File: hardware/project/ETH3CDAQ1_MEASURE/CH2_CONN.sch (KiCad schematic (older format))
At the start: 1 part, among them J1201 Conn_02x10_Odd_Even

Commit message: PCB layout
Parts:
- renumbered J1201 to J1101
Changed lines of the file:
@@
 AR Path="/5FC84995/5FE331B2" Ref="J?"  Part="1"
 AR Path="/5FDF6197/5FE331B2" Ref="J?"  Part="1"
-AR Path="/5FE2FF08/5FE331B2" Ref="J1201"  Part="1"
-F 0 "J1201" H 5400 3517 50  0000 C CNN
+AR Path="/5FE2FF08/5FE331B2" Ref="J1101"  Part="1"
+F 0 "J1101" H 5400 3517 50  0000 C CNN
 F 1 "Conn_02x10_Odd_Even" H 5400 3426 50  0000 C CNN
 F 2 "Connector_PinSocket_2.54mm:PinSocket_2x10_P2.54mm_Vertical" H 5350 2900 50  0001 C CNN
@@
 P 5150 2600
 AR Path="/5FDF6197/5FE331B8" Ref="#PWR?"  Part="1"
-AR Path="/5FE2FF08/5FE331B8" Ref="#PWR01202"  Part="1"
-F 0 "#PWR01202" H 5150 2350 50  0001 C CNN
+AR Path="/5FE2FF08/5FE331B8" Ref="#PWR01102"  Part="1"
+F 0 "#PWR01102" H 5150 2350 50  0001 C CNN
 F 1 "GND" V 5150 2450 50  0000 R CNN
 F 2 "" H 5150 2600 50  0001 C CNN
@@
 P 5150 2700
 AR Path="/5FDF6197/5FE331BE" Ref="#PWR?"  Part="1"
-AR Path="/5FE2FF08/5FE331BE" Ref="#PWR01203"  Part="1"
-F 0 "#PWR01203" H 5150 2450 50  0001 C CNN
+AR Path="/5FE2FF08/5FE331BE" Ref="#PWR01103"  Part="1"
+F 0 "#PWR01103" H 5150 2450 50  0001 C CNN
 F 1 "GND" V 5150 2550 50  0000 R CNN
 F 2 "" H 5150 2700 50  0001 C CNN
@@
 P 5650 2700
 AR Path="/5FDF6197/5FE331C4" Ref="#PWR?"  Part="1"
-AR Path="/5FE2FF08/5FE331C4" Ref="#PWR01208"  Part="1"
-F 0 "#PWR01208" H 5650 2450 50  0001 C CNN
+AR Path="/5FE2FF08/5FE331C4" Ref="#PWR01108"  Part="1"
+F 0 "#PWR01108" H 5650 2450 50  0001 C CNN
 F 1 "GND" V 5650 2550 50  0000 R CNN
 F 2 "" H 5650 2700 50  0001 C CNN
@@
 P 5150 2500
 AR Path="/5FDF6197/5FE331CA" Ref="#PWR?"  Part="1"
-AR Path="/5FE2FF08/5FE331CA" Ref="#PWR01201"  Part="1"
-F 0 "#PWR01201" H 5150 2250 50  0001 C CNN
+AR Path="/5FE2FF08/5FE331CA" Ref="#PWR01101"  Part="1"
+F 0 "#PWR01101" H 5150 2250 50  0001 C CNN
 F 1 "GND" V 5150 2350 50  0000 R CNN
 F 2 "" H 5150 2500 50  0001 C CNN
@@
 P 5150 3100
 AR Path="/5FDF6197/5FE331E4" Ref="#PWR?"  Part="1"
-AR Path="/5FE2FF08/5FE331E4" Ref="#PWR01204"  Part="1"
-F 0 "#PWR01204" H 5150 2850 50  0001 C CNN
+AR Path="/5FE2FF08/5FE331E4" Ref="#PWR01104"  Part="1"
+F 0 "#PWR01104" H 5150 2850 50  0001 C CNN
 F 1 "GND" V 5150 2950 50  0000 R CNN
 F 2 "" H 5150 3100 50  0001 C CNN
@@
 P 5650 3100
 AR Path="/5FDF6197/5FE331EA" Ref="#PWR?"  Part="1"
-AR Path="/5FE2FF08/5FE331EA" Ref="#PWR01209"  Part="1"
-F 0 "#PWR01209" H 5650 2850 50  0001 C CNN
+AR Path="/5FE2FF08/5FE331EA" Ref="#PWR01109"  Part="1"
+F 0 "#PWR01109" H 5650 2850 50  0001 C CNN
 F 1 "GND" V 5650 2950 50  0000 R CNN
 F 2 "" H 5650 3100 50  0001 C CNN
@@
 P 5150 3200
 AR Path="/5FDF6197/5FE331F0" Ref="#PWR?"  Part="1"
-AR Path="/5FE2FF08/5FE331F0" Ref="#PWR01205"  Part="1"
-F 0 "#PWR01205" H 5150 3050 50  0001 C CNN
+AR Path="/5FE2FF08/5FE331F0" Ref="#PWR01105"  Part="1"
+F 0 "#PWR01105" H 5150 3050 50  0001 C CNN
 F 1 "+3.3V" V 5150 3350 50  0000 L CNN
 F 2 "" H 5150 3200 50  0001 C CNN
@@
 P 5650 3200
 AR Path="/5FDF6197/5FE331F6" Ref="#PWR?"  Part="1"
-AR Path="/5FE2FF08/5FE331F6" Ref="#PWR01210"  Part="1"
-F 0 "#PWR01210" H 5650 3050 50  0001 C CNN
+AR Path="/5FE2FF08/5FE331F6" Ref="#PWR01110"  Part="1"
+F 0 "#PWR01110" H 5650 3050 50  0001 C CNN
 F 1 "+3.3V" V 5650 3350 50  0000 L CNN
 F 2 "" H 5650 3200 50  0001 C CNN
@@
 P 5150 3300
 AR Path="/5FDF6197/5FE331FC" Ref="#PWR?"  Part="1"
-AR Path="/5FE2FF08/5FE331FC" Ref="#PWR01206"  Part="1"
-F 0 "#PWR01206" H 5150 3150 50  0001 C CNN
+AR Path="/5FE2FF08/5FE331FC" Ref="#PWR01106"  Part="1"
+F 0 "#PWR01106" H 5150 3150 50  0001 C CNN
 F 1 "+9V" V 5150 3450 50  0000 L CNN
 F 2 "" H 5150 3300 50  0001 C CNN
@@
 P 5650 3300
 AR Path="/5FDF6197/5FE33202" Ref="#PWR?"  Part="1"
-AR Path="/5FE2FF08/5FE33202" Ref="#PWR01211"  Part="1"
-F 0 "#PWR01211" H 5650 3150 50  0001 C CNN
+AR Path="/5FE2FF08/5FE33202" Ref="#PWR01111"  Part="1"
+F 0 "#PWR01111" H 5650 3150 50  0001 C CNN
 F 1 "+5V" V 5650 3450 50  0000 L CNN
 F 2 "" H 5650 3300 50  0001 C CNN
@@
 P 5150 3400
 AR Path="/5FDF6197/5FE33208" Ref="#PWR?"  Part="1"
-AR Path="/5FE2FF08/5FE33208" Ref="#PWR01207"  Part="1"
-F 0 "#PWR01207" H 5150 3250 50  0001 C CNN
+AR Path="/5FE2FF08/5FE33208" Ref="#PWR01107"  Part="1"
+F 0 "#PWR01107" H 5150 3250 50  0001 C CNN
 F 1 "-18V" V 5150 3550 50  0000 L CNN
 F 2 "" H 5150 3400 50  0001 C CNN
@@
 P 5650 3400
 AR Path="/5FDF6197/5FE3320E" Ref="#PWR?"  Part="1"
-AR Path="/5FE2FF08/5FE3320E" Ref="#PWR01212"  Part="1"
-F 0 "#PWR01212" H 5650 3250 50  0001 C CNN
+AR Path="/5FE2FF08/5FE3320E" Ref="#PWR01112"  Part="1"
+F 0 "#PWR01112" H 5650 3250 50  0001 C CNN
 F 1 "+18V" V 5650 3550 50  0000 L CNN
 F 2 "" H 5650 3400 50  0001 C CNN

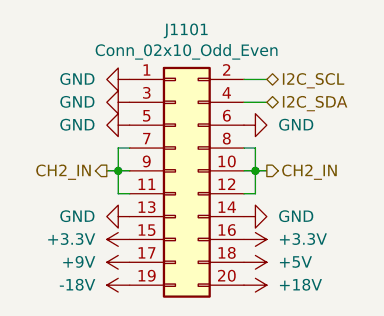
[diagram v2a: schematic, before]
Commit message: Started development of first current measurement module. Added CAN to the DAQ module.
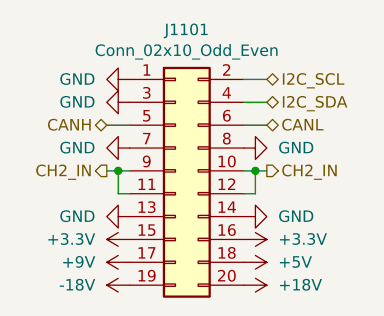
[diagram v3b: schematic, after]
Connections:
- net CH2_IN: no longer J1101.7 (Pin_7), J1101.8 (Pin_8)
- net GND: now also J1101.7 (Pin_7), J1101.8 (Pin_8); no longer J1101.5 (Pin_5), J1101.6 (Pin_6)
- new net CANH: J1101.5 (Pin_5)
- new net CANL: J1101.6 (Pin_6)
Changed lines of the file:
@@
 $Descr A4 11693 8268
 encoding utf-8
-Sheet 12 15
+Sheet 11 15
 Title ""
 Date ""
@@
 	0    1    1    0
 $EndComp
-$Comp
-L power:GND #PWR?
-U 1 1 5FE331BE
-P 5150 2700
-AR Path="/5FDF6197/5FE331BE" Ref="#PWR?"  Part="1"
-AR Path="/5FE2FF08/5FE331BE" Ref="#PWR01103"  Part="1"
-F 0 "#PWR01103" H 5150 2450 50  0001 C CNN
-F 1 "GND" V 5150 2550 50  0000 R CNN
-F 2 "" H 5150 2700 50  0001 C CNN
-F 3 "" H 5150 2700 50  0001 C CNN
-	1    5150 2700
-	0    1    1    0
-$EndComp
-$Comp
-L power:GND #PWR?
-U 1 1 5FE331C4
-P 5650 2700
-AR Path="/5FDF6197/5FE331C4" Ref="#PWR?"  Part="1"
-AR Path="/5FE2FF08/5FE331C4" Ref="#PWR01108"  Part="1"
-F 0 "#PWR01108" H 5650 2450 50  0001 C CNN
-F 1 "GND" V 5650 2550 50  0000 R CNN
-F 2 "" H 5650 2700 50  0001 C CNN
-F 3 "" H 5650 2700 50  0001 C CNN
-	1    5650 2700
-	0    -1   -1   0
-$EndComp
-$Comp
-L power:GND #PWR?
-U 1 1 5FE331CA
-P 5150 2500
-AR Path="/5FDF6197/5FE331CA" Ref="#PWR?"  Part="1"
-AR Path="/5FE2FF08/5FE331CA" Ref="#PWR01101"  Part="1"
-F 0 "#PWR01101" H 5150 2250 50  0001 C CNN
-F 1 "GND" V 5150 2350 50  0000 R CNN
-F 2 "" H 5150 2500 50  0001 C CNN
-F 3 "" H 5150 2500 50  0001 C CNN
-	1    5150 2500
-	0    1    1    0
-$EndComp
 Text HLabel 5750 2500 2    50   BiDi ~ 0
 I2C_SCL
@@
 	5650 2500 5750 2500
 Wire Wire Line
-	5650 2800 5700 2800
-Wire Wire Line
-	5700 2800 5700 2900
-Wire Wire Line
 	5700 3000 5650 3000
 Wire Wire Line
@@
 Wire Wire Line
 	5700 2900 5700 3000
-Wire Wire Line
-	5150 2800 5100 2800
-Wire Wire Line
-	5100 2800 5100 2900
 Wire Wire Line
 	5100 3000 5150 3000
@@
 	0    1    1    0
 $EndComp
+Wire Wire Line
+	5650 2700 5750 2700
+Wire Wire Line
+	5150 2700 5050 2700
+Text HLabel 5050 2700 0    50   BiDi ~ 0
+CANH
+Text HLabel 5750 2700 2    50   BiDi ~ 0
+CANL
+$Comp
+L power:GND #PWR?
+U 1 1 5FE5AC8A
+P 5150 2800
+AR Path="/5FDF6197/5FE5AC8A" Ref="#PWR?"  Part="1"
+AR Path="/5FE2FF08/5FE5AC8A" Ref="#PWR01103"  Part="1"
+F 0 "#PWR01103" H 5150 2550 50  0001 C CNN
+F 1 "GND" V 5150 2650 50  0000 R CNN
+F 2 "" H 5150 2800 50  0001 C CNN
+F 3 "" H 5150 2800 50  0001 C CNN
+	1    5150 2800
+	0    1    1    0
+$EndComp
+$Comp
+L power:GND #PWR?
+U 1 1 5FE5AE75
+P 5650 2800
+AR Path="/5FDF6197/5FE5AE75" Ref="#PWR?"  Part="1"
+AR Path="/5FE2FF08/5FE5AE75" Ref="#PWR01108"  Part="1"
+F 0 "#PWR01108" H 5650 2550 50  0001 C CNN
+F 1 "GND" V 5650 2650 50  0000 R CNN
+F 2 "" H 5650 2800 50  0001 C CNN
+F 3 "" H 5650 2800 50  0001 C CNN
+	1    5650 2800
+	0    -1   -1   0
+$EndComp
+$Comp
+L power:GND #PWR?
+U 1 1 5FE5EED1
+P 5150 2500
+AR Path="/5FDF6197/5FE5EED1" Ref="#PWR?"  Part="1"
+AR Path="/5FE2FF08/5FE5EED1" Ref="#PWR01101"  Part="1"
+F 0 "#PWR01101" H 5150 2250 50  0001 C CNN
+F 1 "GND" V 5150 2350 50  0000 R CNN
+F 2 "" H 5150 2500 50  0001 C CNN
+F 3 "" H 5150 2500 50  0001 C CNN
+	1    5150 2500
+	0    1    1    0
+$EndComp
